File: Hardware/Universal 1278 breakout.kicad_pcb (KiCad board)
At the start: 2 copper layers, 26.7 x 30.6 mm, 7 parts, among them J2 Conn_01x10, J3 Conn_01x10, U2 DRF1278F

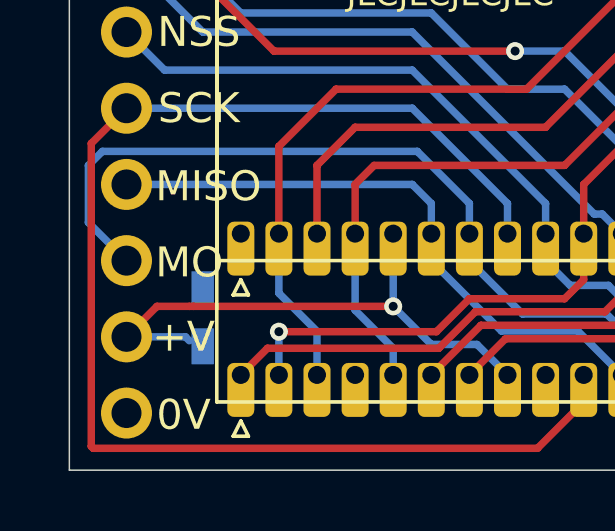
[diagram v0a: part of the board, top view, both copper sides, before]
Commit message: Fix (most) DRC errors.
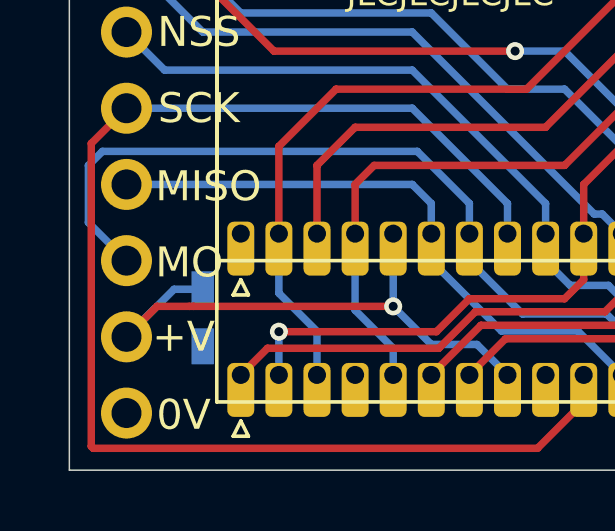
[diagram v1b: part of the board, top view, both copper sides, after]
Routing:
- net VCC: track 18.6 -> 19.7 mm

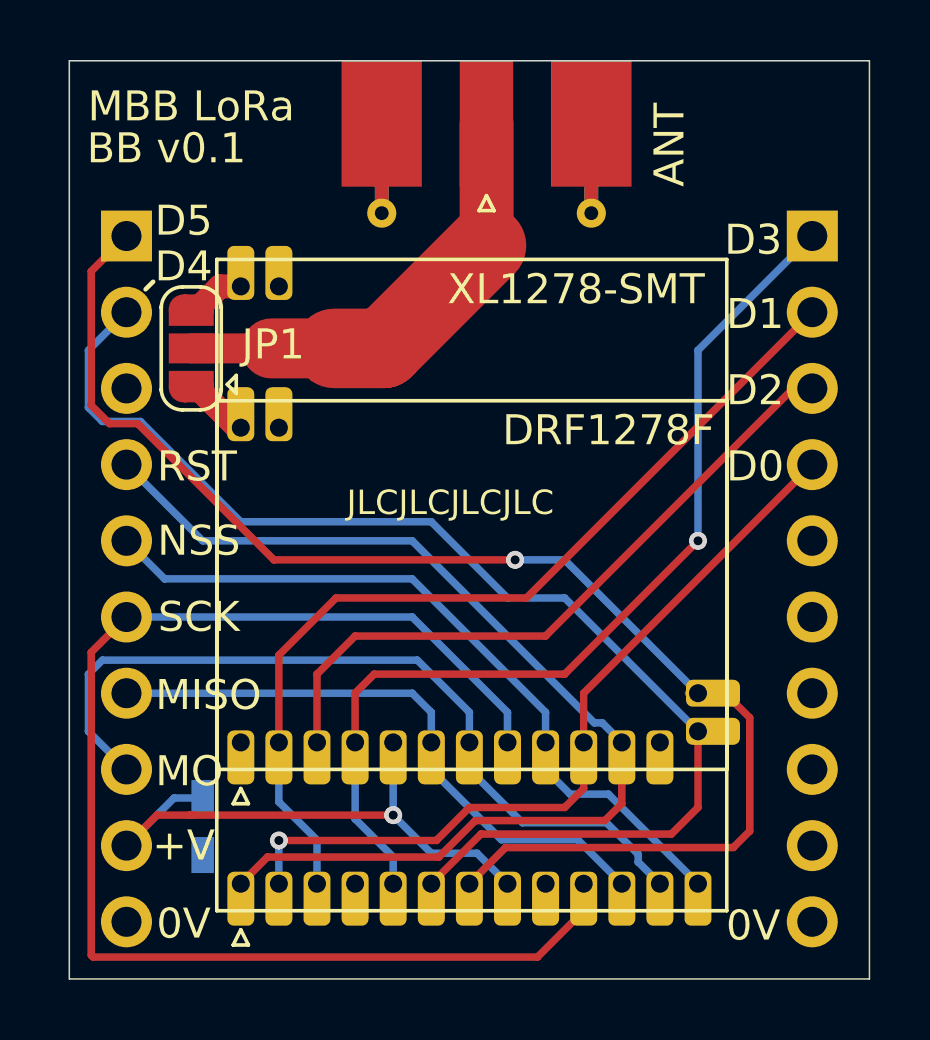
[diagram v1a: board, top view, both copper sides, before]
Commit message: Ground pour. All DRC errors fixed except courtyards. Ignore courtyard warnings.
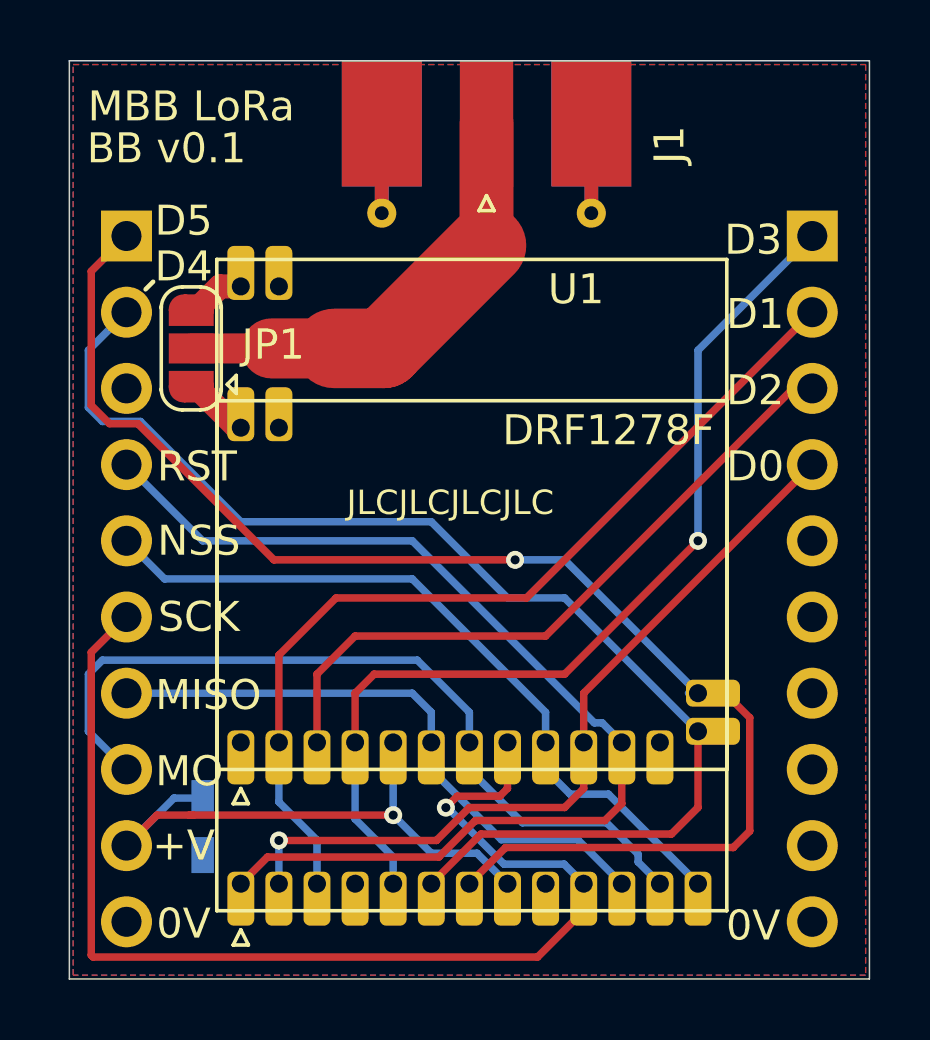
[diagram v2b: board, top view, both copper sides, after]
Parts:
- renumbered ANT to J1, XL1278-SMT to U1
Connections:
- J1 pad 2: Net-(J1-Pad2) -> GND
- U1 pad 15: Net-(J1-Pad2) -> GND
- U2 pad 14: Net-(J1-Pad2) -> GND
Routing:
- net SCK: track 44.8 -> 39.3 mm, vias 0 -> 1
- added copper zone on B.Cu, net GND
- added copper zone on F.Cu, net GND
